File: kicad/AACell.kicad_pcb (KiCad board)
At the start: 2 copper layers, 14.2 x 78.6 mm, 9 parts, among them CON1 USB-MICRO-B, U1 TPS776xx

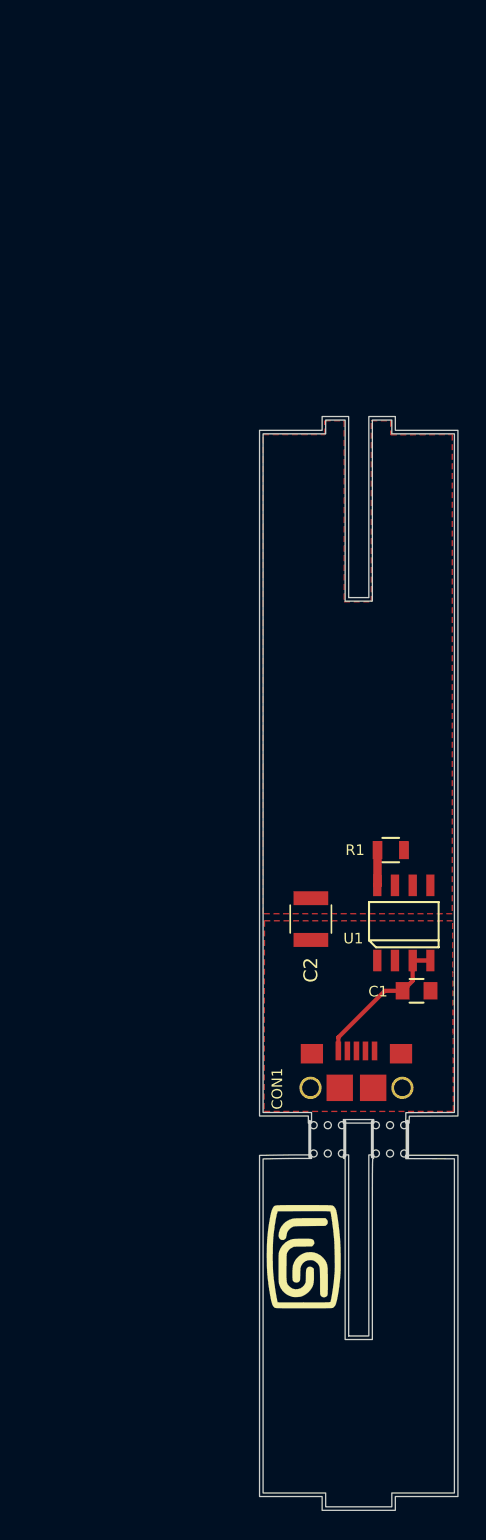
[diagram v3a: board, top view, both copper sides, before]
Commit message: Changes the layout and mouse-bites arrangement to ensure + pole pads and 2 layers
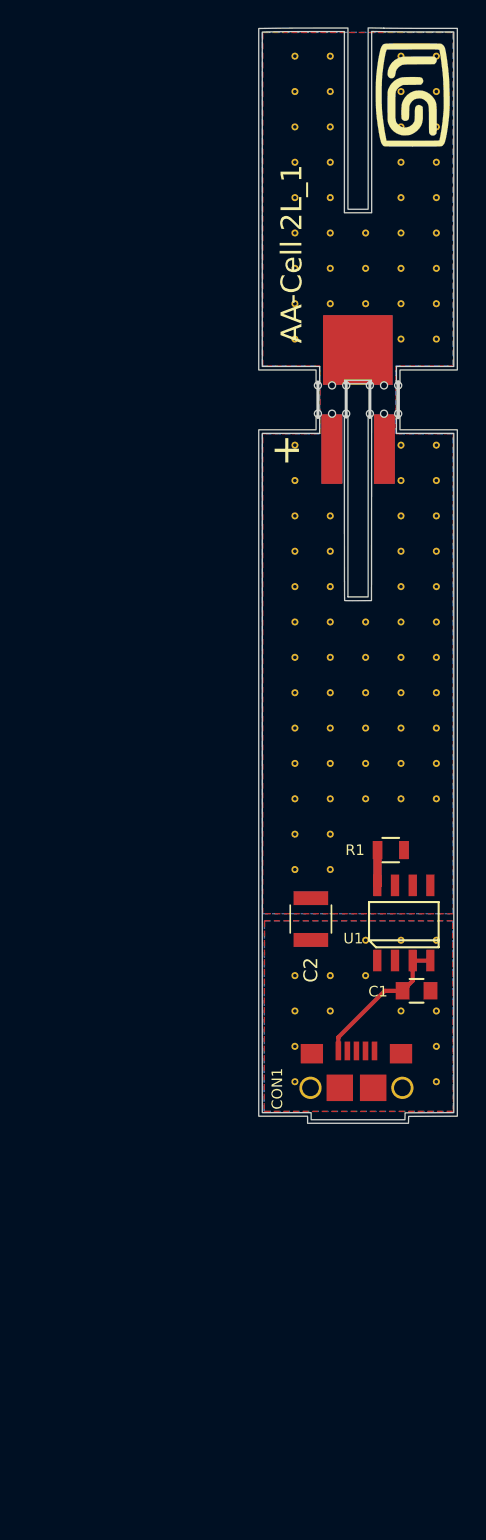
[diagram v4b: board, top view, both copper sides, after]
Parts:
- added ?: , AACell-Footprint:SJM_7mm, B.Cu at (118.6, 82.4)
- added ?: , AACell-Footprint:STITCH_VIA, F.Cu at (116.8, 94.0)
- added ?: , AACell-Footprint:STITCH_VIA, F.Cu at (119.4, 22.9)
- added ?: , AACell-Footprint:STITCH_VIA, F.Cu at (116.8, 22.9)
- added ?: , AACell-Footprint:STITCH_VIA, F.Cu at (127.0, 20.3)
- added ?: , AACell-Footprint:STITCH_VIA, F.Cu at (124.5, 20.3)
- added ?: , AACell-Footprint:STITCH_VIA, F.Cu at (119.4, 20.3)
- added ?: , AACell-Footprint:STITCH_VIA, F.Cu at (116.8, 20.3)
- added ?: , AACell-Footprint:Terminal, F.Cu at (121.4, 41.4)
- added ?: , AACell-Footprint:STITCH_VIA, F.Cu at (116.8, 91.4)
- added ?: , AACell-Footprint:STITCH_VIA, F.Cu at (116.8, 88.9)
- added ?: , AACell-Footprint:STITCH_VIA, F.Cu at (119.4, 88.9)
- added ?: , AACell-Footprint:STITCH_VIA, F.Cu at (119.4, 86.4)
- added ?: , AACell-Footprint:STITCH_VIA, F.Cu at (116.8, 86.4)
- added ?: , AACell-Footprint:STITCH_VIA, F.Cu at (119.4, 76.2)
- added ?: , AACell-Footprint:STITCH_VIA, F.Cu at (116.8, 78.7)
- added ?: , AACell-Footprint:STITCH_VIA, F.Cu at (116.8, 76.2)
- added ?: , AACell-Footprint:STITCH_VIA, F.Cu at (119.4, 78.7)
- added ?: , AACell-Footprint:STITCH_VIA, F.Cu at (121.9, 86.4)
- added ?: , AACell-Footprint:STITCH_VIA, F.Cu at (121.9, 73.7)
- added ?: , AACell-Footprint:STITCH_VIA, F.Cu at (116.8, 73.7)
- added ?: , AACell-Footprint:STITCH_VIA, F.Cu at (121.9, 71.1)
- added ?: , AACell-Footprint:STITCH_VIA, F.Cu at (119.4, 71.1)
- added ?: , AACell-Footprint:STITCH_VIA, F.Cu at (116.8, 71.1)
- added ?: , AACell-Footprint:STITCH_VIA, F.Cu at (119.4, 73.7)
- added ?: , AACell-Footprint:STITCH_VIA, F.Cu at (127.0, 73.7)
- added ?: , AACell-Footprint:STITCH_VIA, F.Cu at (124.5, 71.1)
- added ?: , AACell-Footprint:STITCH_VIA, F.Cu at (127.0, 71.1)
- added ?: , AACell-Footprint:STITCH_VIA, F.Cu at (124.5, 73.7)
- added ?: , AACell-Footprint:STITCH_VIA, F.Cu at (121.9, 83.8)
- added ?: , AACell-Footprint:STITCH_VIA, F.Cu at (127.0, 68.6)
- added ?: , AACell-Footprint:STITCH_VIA, F.Cu at (124.5, 68.6)
- added ?: , AACell-Footprint:STITCH_VIA, F.Cu at (121.9, 68.6)
- added ?: , AACell-Footprint:STITCH_VIA, F.Cu at (119.4, 68.6)
- added ?: , AACell-Footprint:STITCH_VIA, F.Cu at (116.8, 68.6)
- added ?: , AACell-Footprint:STITCH_VIA, F.Cu at (127.0, 66.0)
- added ?: , AACell-Footprint:STITCH_VIA, F.Cu at (124.5, 66.0)
- added ?: , AACell-Footprint:STITCH_VIA, F.Cu at (121.9, 66.0)
- added ?: , AACell-Footprint:STITCH_VIA, F.Cu at (119.4, 66.0)
- added ?: , AACell-Footprint:STITCH_VIA, F.Cu at (116.8, 66.0)
- added ?: , AACell-Footprint:STITCH_VIA, F.Cu at (124.5, 83.8)
- added ?: , AACell-Footprint:STITCH_VIA, F.Cu at (127.0, 63.5)
- added ?: , AACell-Footprint:STITCH_VIA, F.Cu at (124.5, 63.5)
- added ?: , AACell-Footprint:STITCH_VIA, F.Cu at (121.9, 63.5)
- added ?: , AACell-Footprint:STITCH_VIA, F.Cu at (119.4, 63.5)
- added ?: , AACell-Footprint:STITCH_VIA, F.Cu at (116.8, 63.5)
- added ?: , AACell-Footprint:STITCH_VIA, F.Cu at (127.0, 61.0)
- added ?: , AACell-Footprint:STITCH_VIA, F.Cu at (124.5, 61.0)
- added ?: , AACell-Footprint:STITCH_VIA, F.Cu at (121.9, 61.0)
- added ?: , AACell-Footprint:STITCH_VIA, F.Cu at (119.4, 61.0)
- added ?: , AACell-Footprint:STITCH_VIA, F.Cu at (116.8, 61.0)
- added ?: , AACell-Footprint:STITCH_VIA, F.Cu at (127.0, 83.8)
- added ?: , AACell-Footprint:STITCH_VIA, F.Cu at (127.0, 58.4)
- added ?: , AACell-Footprint:STITCH_VIA, F.Cu at (124.5, 58.4)
- added ?: , AACell-Footprint:STITCH_VIA, F.Cu at (119.4, 58.4)
- added ?: , AACell-Footprint:STITCH_VIA, F.Cu at (116.8, 58.4)
- added ?: , AACell-Footprint:STITCH_VIA, F.Cu at (127.0, 55.9)
- added ?: , AACell-Footprint:STITCH_VIA, F.Cu at (124.5, 55.9)
- added ?: , AACell-Footprint:STITCH_VIA, F.Cu at (119.4, 55.9)
- added ?: , AACell-Footprint:STITCH_VIA, F.Cu at (116.8, 55.9)
- added ?: , AACell-Footprint:STITCH_VIA, F.Cu at (127.0, 53.3)
- added ?: , AACell-Footprint:STITCH_VIA, F.Cu at (124.5, 53.3)
- added ?: , AACell-Footprint:STITCH_VIA, F.Cu at (127.0, 88.9)
- added ?: , AACell-Footprint:STITCH_VIA, F.Cu at (119.4, 53.3)
- added ?: , AACell-Footprint:STITCH_VIA, F.Cu at (116.8, 53.3)
- added ?: , AACell-Footprint:STITCH_VIA, F.Cu at (127.0, 50.8)
- added ?: , AACell-Footprint:STITCH_VIA, F.Cu at (124.5, 50.8)
- added ?: , AACell-Footprint:STITCH_VIA, F.Cu at (116.8, 50.8)
- added ?: , AACell-Footprint:STITCH_VIA, F.Cu at (127.0, 48.3)
- added ?: , AACell-Footprint:STITCH_VIA, F.Cu at (124.5, 48.3)
- added ?: , AACell-Footprint:STITCH_VIA, F.Cu at (116.8, 48.3)
- added ?: , AACell-Footprint:STITCH_VIA, F.Cu at (127.0, 40.6)
- added ?: , AACell-Footprint:STITCH_VIA, F.Cu at (124.5, 40.6)
- added ?: , AACell-Footprint:STITCH_VIA, F.Cu at (124.5, 88.9)
- added ?: , AACell-Footprint:STITCH_VIA, F.Cu at (116.8, 40.6)
- added ?: , AACell-Footprint:STITCH_VIA, F.Cu at (127.0, 38.1)
- added ?: , AACell-Footprint:STITCH_VIA, F.Cu at (124.5, 38.1)
- added ?: , AACell-Footprint:STITCH_VIA, F.Cu at (121.9, 38.1)
- added ?: , AACell-Footprint:STITCH_VIA, F.Cu at (119.4, 38.1)
- added ?: , AACell-Footprint:STITCH_VIA, F.Cu at (116.8, 38.1)
- added ?: , AACell-Footprint:STITCH_VIA, F.Cu at (127.0, 35.6)
- added ?: , AACell-Footprint:STITCH_VIA, F.Cu at (124.5, 35.6)
- added ?: , AACell-Footprint:STITCH_VIA, F.Cu at (121.9, 35.6)
- added ?: , AACell-Footprint:STITCH_VIA, F.Cu at (119.4, 35.6)
- added ?: , AACell-Footprint:STITCH_VIA, F.Cu at (127.0, 91.4)
- added ?: , AACell-Footprint:STITCH_VIA, F.Cu at (116.8, 35.6)
- added ?: , AACell-Footprint:STITCH_VIA, F.Cu at (127.0, 33.0)
- added ?: , AACell-Footprint:STITCH_VIA, F.Cu at (124.5, 33.0)
- added ?: , AACell-Footprint:STITCH_VIA, F.Cu at (121.9, 33.0)
- added ?: , AACell-Footprint:STITCH_VIA, F.Cu at (119.4, 33.0)
- added ?: , AACell-Footprint:STITCH_VIA, F.Cu at (116.8, 33.0)
- added ?: , AACell-Footprint:STITCH_VIA, F.Cu at (127.0, 30.5)
- added ?: , AACell-Footprint:STITCH_VIA, F.Cu at (124.5, 30.5)
- added ?: , AACell-Footprint:STITCH_VIA, F.Cu at (119.4, 30.5)
- added ?: , AACell-Footprint:STITCH_VIA, F.Cu at (116.8, 30.5)
- added ?: , AACell-Footprint:STITCH_VIA, F.Cu at (127.0, 94.0)
- added ?: , AACell-Footprint:STITCH_VIA, F.Cu at (127.0, 27.9)
- added ?: , AACell-Footprint:STITCH_VIA, F.Cu at (124.5, 27.9)
- added ?: , AACell-Footprint:STITCH_VIA, F.Cu at (119.4, 27.9)
- added ?: , AACell-Footprint:STITCH_VIA, F.Cu at (116.8, 27.9)
- added ?: , AACell-Footprint:STITCH_VIA, F.Cu at (127.0, 25.4)
- added ?: , AACell-Footprint:STITCH_VIA, F.Cu at (124.5, 25.4)
- added ?: , AACell-Footprint:STITCH_VIA, F.Cu at (119.4, 25.4)
- added ?: , AACell-Footprint:STITCH_VIA, F.Cu at (116.8, 25.4)
- added ?: , AACell-Footprint:STITCH_VIA, F.Cu at (127.0, 22.9)
- added ?: , AACell-Footprint:STITCH_VIA, F.Cu at (124.5, 22.9)
- added REF**: Terminal, AACell-Footprint:Terminal-Split, F.Cu at (119.5, 48.5)
- ?: renamed from G***; value LOGO -> (none)
- moved ? 83.8 mm to (125.3, 23.1)
- moved REF** 53.1 mm to (123.2, 45.0)
- moved REF** 53.1 mm to (119.5, 45.0)
- moved B*** 27.8 mm to (121.4, 57.6)
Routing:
- added copper zone on B.Cu, net /VOUT
- added copper zone on B.Cu, net GND
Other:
- board size 14.2 x 78.6 mm -> 14.3 x 78.7 mm
- board text added: "+"
- board text added: "AA-Cell 2L_1"

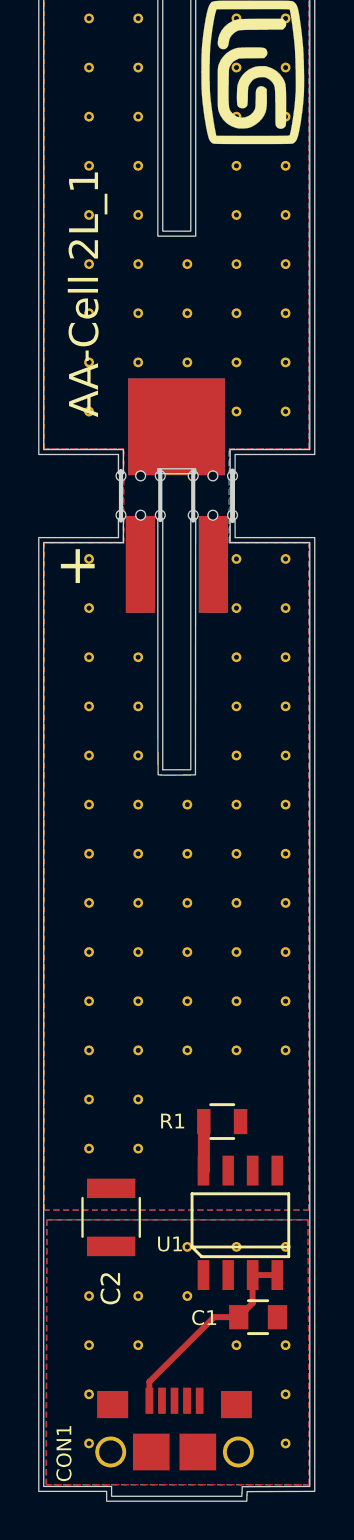
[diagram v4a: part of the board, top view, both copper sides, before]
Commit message: AA-Cell 2L_2 based on the ADP3339AKCZ-1.5-R7 submitted to OSH Park
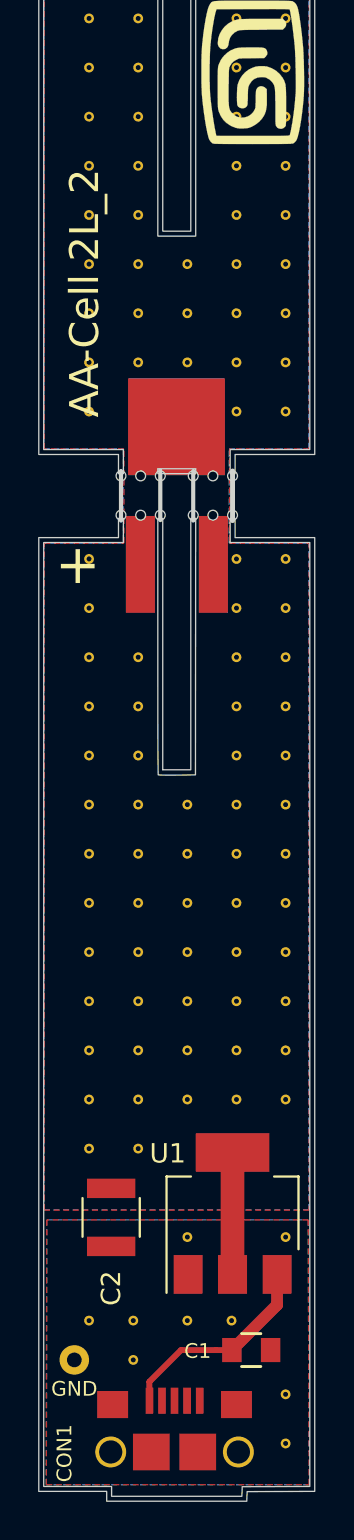
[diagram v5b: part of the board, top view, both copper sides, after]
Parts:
- removed the ? at (116.8, 94.0)
- removed the ? at (116.8, 91.4)
- removed the ? at (116.8, 88.9)
- removed the ? at (119.4, 88.9)
- removed the ? at (119.4, 86.4)
- removed the ? at (116.8, 86.4)
- removed the ? at (124.5, 83.8)
- removed the ? at (127.0, 88.9)
- removed the ? at (124.5, 88.9)
- removed R1: 250kΩ, Resistors_SMD:R_0805
- added ?: , AACell-Footprint:STITCH_VIA, F.Cu at (119.1, 89.7)
- added ?: , AACell-Footprint:STITCH_VIA, F.Cu at (116.8, 87.6)
- added ?: , AACell-Footprint:STITCH_VIA, F.Cu at (119.1, 87.6)
- added ?: , AACell-Footprint:STITCH_VIA, F.Cu at (121.9, 76.2)
- added ?: , AACell-Footprint:STITCH_VIA, F.Cu at (124.5, 76.2)
- added ?: , AACell-Footprint:STITCH_VIA, F.Cu at (127.0, 76.2)
- added ?: , AACell-Footprint:STITCH_VIA, F.Cu at (124.2, 87.6)
- added GND: , AACell-Footprint:GND_Connect, F.Cu at (116.1, 89.7)
- C1: value 0.1μF -> 1μF
- C2: value 10μF -> 1μF
- U1: value TPS776xx -> ADP3339AKCZ-1.5-R7; footprint AACell-Footprint:SOIC_5.4_1.27 -> TO_SOT_Packages_SMD:SOT-223
- moved C1 1.74 mm to (125.2, 89.2)
- moved ? 1.35 mm to (118.6, 81.0)
- moved ? 1.27 mm to (121.9, 87.6)
- moved U1 0.63 mm to (124.3, 82.1), turned to 90 degrees
- moved ? 0.51 mm to (121.9, 83.3)
- moved ? 0.51 mm to (127.0, 83.3)
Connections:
- U1 pad 2: GND -> /VOUT
- U1 pad 4: Net-(C1-Pad1) -> /VOUT
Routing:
- net /VOUT: track 0.00 -> 6.30 mm
- net /~RESET~/PG: track 2.54 -> 0.00 mm
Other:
- board text added: "AA-Cell 2L_2"
- board text removed: "AA-Cell 2L_1"
